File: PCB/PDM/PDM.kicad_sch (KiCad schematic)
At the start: 16 parts, among them IC3 SN65HVD230QDG4Q1, IC4 TS5A21366DCUR, IC5 TMP126NDCKR, IC6 TMP126NDCKR, IC9 SN65HVD230QDG4Q1, J1 Conn_01x01_Male

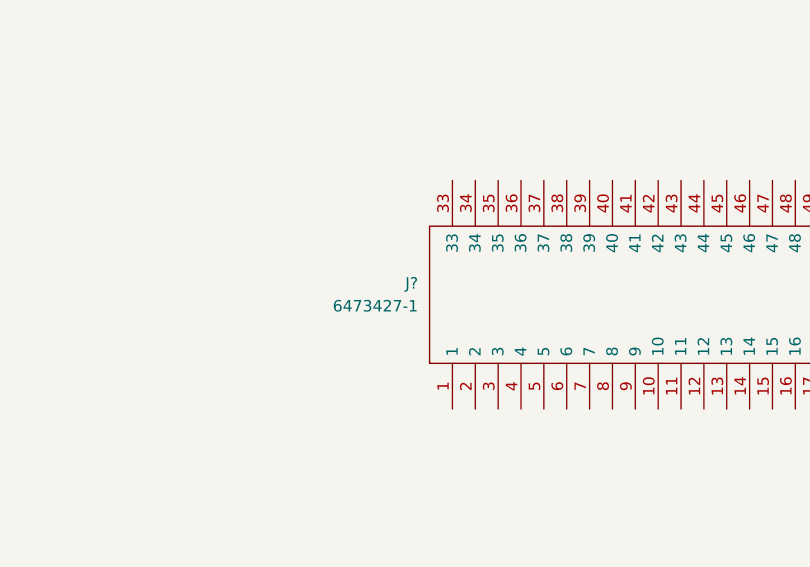
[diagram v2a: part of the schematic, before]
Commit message: Added fuse on each output of hs section - change footprint later!
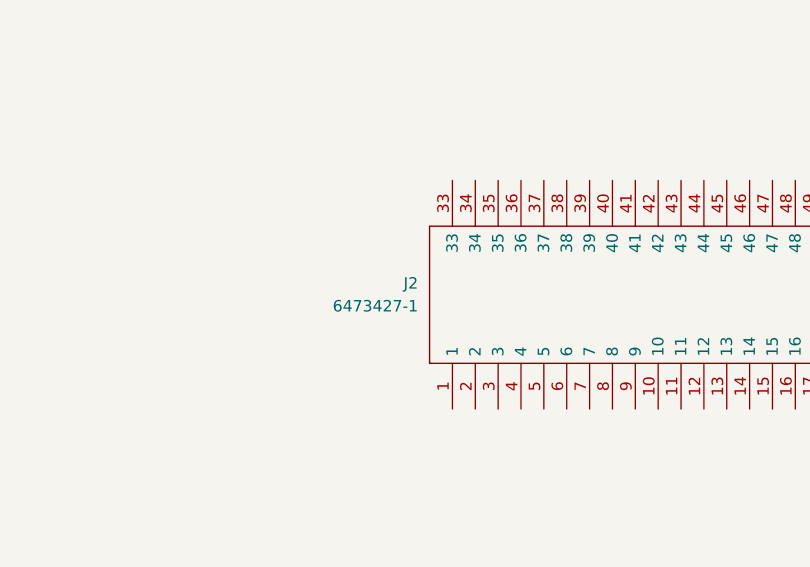
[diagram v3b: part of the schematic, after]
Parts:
- J2: renamed from J?; footprint 64734271 -> PDM_Additional:64734271
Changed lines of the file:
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@@
   (symbol (lib_id "PDM_additional:6473427-1") (at 264.16 234.95 90) (unit 1)
     (in_bom yes) (on_board yes) (fields_autoplaced)
-    (property "Reference" "J?" (id 0) (at 260.35 220.9799 90)
+    (property "Reference" "J2" (id 0) (at 260.35 220.9799 90)
       (effects (font (size 1.27 1.27)) (justify left))
     )
@@
       (effects (font (size 1.27 1.27)) (justify left))
     )
-    (property "Footprint" "64734271" (id 2) (at 261.62 213.36 0)
+    (property "Footprint" "PDM_Additional:64734271" (id 2) (at 261.62 213.36 0)
       (effects (font (size 1.27 1.27)) (justify left) hide)
     )
@@
       (reference "D19") (unit 1) (value "WS2812B") (footprint "LED_SMD:LED_WS2812B-2020_PLCC4_2.0x2.0mm")
     )
+    (path "/46244c59-2e4b-42a4-823a-85726f18505b/b2f362ca-79e9-4719-b603-d3d2d0d8335e/c25a33e2-a80b-47b2-9a70-9b1c3a189cb0"
+      (reference "F1") (unit 1) (value "40A") (footprint "Fuse:Fuse_2512_6332Metric")
+    )
+    (path "/46244c59-2e4b-42a4-823a-85726f18505b/e8b0a6e4-c2f9-4e16-af84-64c9badf4bf1/c25a33e2-a80b-47b2-9a70-9b1c3a189cb0"
+      (reference "F2") (unit 1) (value "40A") (footprint "Fuse:Fuse_2512_6332Metric")
+    )
+    (path "/46244c59-2e4b-42a4-823a-85726f18505b/321b0039-eb18-4da2-a831-1121bf986851/c25a33e2-a80b-47b2-9a70-9b1c3a189cb0"
+      (reference "F3") (unit 1) (value "40A") (footprint "Fuse:Fuse_2512_6332Metric")
+    )
+    (path "/46244c59-2e4b-42a4-823a-85726f18505b/5bf8b725-240e-412e-a5c3-5044c753d539/c25a33e2-a80b-47b2-9a70-9b1c3a189cb0"
+      (reference "F4") (unit 1) (value "40A") (footprint "Fuse:Fuse_2512_6332Metric")
+    )
+    (path "/46244c59-2e4b-42a4-823a-85726f18505b/1d5c9ea4-55cc-4fca-bd0f-950f7b88fb67/c25a33e2-a80b-47b2-9a70-9b1c3a189cb0"
+      (reference "F5") (unit 1) (value "40A") (footprint "Fuse:Fuse_2512_6332Metric")
+    )
+    (path "/46244c59-2e4b-42a4-823a-85726f18505b/70742282-285b-4afc-a4d9-22fef2009c04/c25a33e2-a80b-47b2-9a70-9b1c3a189cb0"
+      (reference "F6") (unit 1) (value "40A") (footprint "Fuse:Fuse_2512_6332Metric")
+    )
+    (path "/46244c59-2e4b-42a4-823a-85726f18505b/1bc2fd01-7291-466b-8e7c-215aac36011b/c25a33e2-a80b-47b2-9a70-9b1c3a189cb0"
+      (reference "F7") (unit 1) (value "40A") (footprint "Fuse:Fuse_2512_6332Metric")
+    )
+    (path "/46244c59-2e4b-42a4-823a-85726f18505b/47b8ab21-edd5-494e-8b41-1707eff52f6f/c25a33e2-a80b-47b2-9a70-9b1c3a189cb0"
+      (reference "F8") (unit 1) (value "40A") (footprint "Fuse:Fuse_2512_6332Metric")
+    )
     (path "/f9c327f1-1acc-4362-b996-4cc92af6a1f0/35dc7052-e012-4a38-a52d-01a9bd451b7a"
       (reference "IC1") (unit 1) (value "STM32L496ZGT6") (footprint "PDM_Additional:QFP50P2200X2200X160-144N")
@@
     )
     (path "/ec3ef24a-d14e-4473-a6de-a99822874369"
-      (reference "J?") (unit 1) (value "6473427-1") (footprint "64734271")
+      (reference "J2") (unit 1) (value "6473427-1") (footprint "PDM_Additional:64734271")
     )
     (path "/f9c327f1-1acc-4362-b996-4cc92af6a1f0/f8c11e5d-bead-478c-a036-ba63a8f5504e"

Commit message: Added adc protection and HC header radsock
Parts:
- removed C13: 0,1mF, Capacitor_SMD:C_0805_2012Metric, symbol Device:C_Small
- removed C95, C96: 100nF, Capacitor_SMD:C_0805_2012Metric, symbol Device:C_Small
- removed IC3, IC9: SN65HVD230QDG4Q1, PDM_Additional:SOIC127P600X175-8N, symbol PDM_additional:SN65HVD230QDG4Q1
- removed IC4: TS5A21366DCUR, PDM_Additional:SOP50P310X90-8N, symbol PDM_additional:TS5A21366DCUR
- removed R118, R119: 0, Resistor_SMD:R_0402_1005Metric, symbol Device:R_Small
- removed R16, R17: 120, Resistor_SMD:R_0402_1005Metric, symbol Device:R_Small
- added J3: N01_036_6501_001, PDM_Additional:N010366501001, symbol PDM_additional:N01_036_6501_001
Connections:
- no-connect marks 2 -> 0
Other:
- added sheet CANBUS (canbus.kicad_sch)
- sheet HIGH SIDE1 ports: added none; removed {SPI1}
- note removed: "CAN BUS"
- note removed: "CAN1"
- note removed: "CAN2"
- note removed: "Consider changing to SN65HVD234-Q1 for 3.3V and Q1 cert"
- note removed: "HS mode (0Ohm) or slope selection."
- note removed: "Software termination for CAN1 & CAN2"
- moved on the sheet: IC5, IC6, R18, R19
